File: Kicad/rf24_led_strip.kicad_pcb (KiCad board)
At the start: 2 copper layers, 50 x 50 mm, 85 parts, among them P1 12V in, P11 CONN_01X07, P2 LED_OUT, P3 LED2_OUT, P4 LED3_OUT, P5 LED4_OUT, P6 LED5_OUT, P7 USB_OTG, P8 SWD, P9 UART, Q10 Q_NMOS_GDS, Q11 Q_NMOS_GDS, Q12 Q_NMOS_GDS, Q13 Q_NMOS_GDS, Q14 Q_NMOS_GDS, Q15 Q_NMOS_GDS, Q16 Q_NMOS_GDS, Q2 Q_NMOS_GDS, Q3 Q_NMOS_GDS, Q4 Q_NMOS_GDS, Q5 Q_NMOS_GDS, Q6 Q_NMOS_GDS, Q7 Q_NMOS_GDS, Q8 Q_NMOS_GDS, Q9 Q_NMOS_GDS, U1 nrf24l01+, U2 ESP-01, U3 STM32F103C8Tx, U4 LM_1117, Y1 Crystal

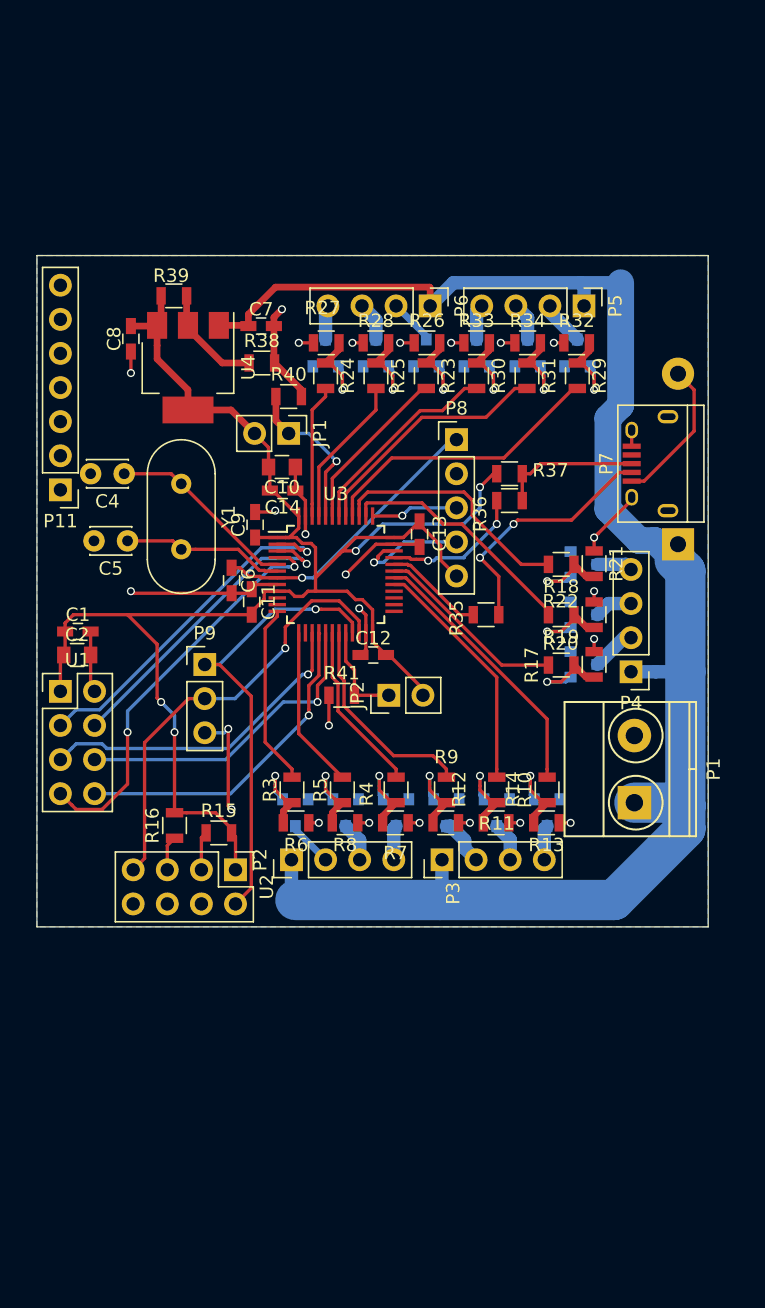
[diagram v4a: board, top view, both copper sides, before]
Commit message: First "complete" stm32 version.
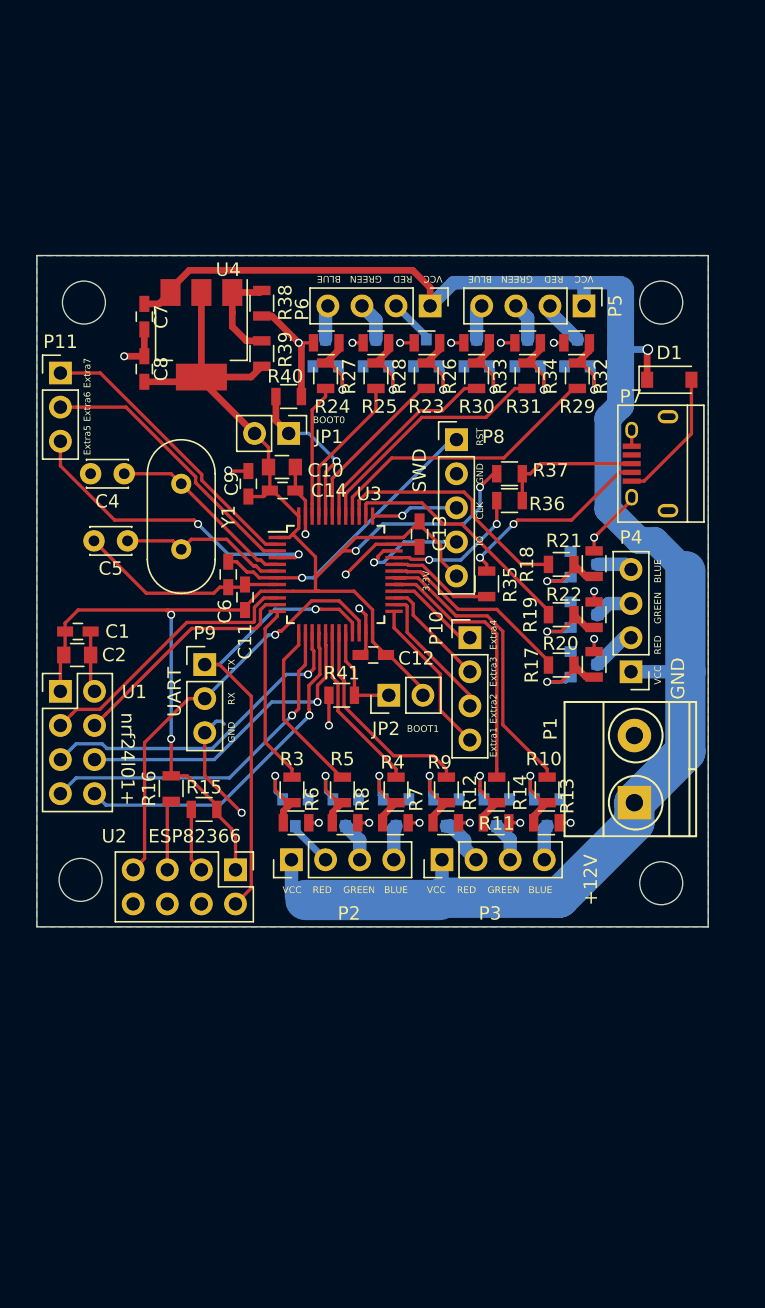
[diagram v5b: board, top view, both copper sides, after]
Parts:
- added P10: CONN_01X04, Pin_Headers:Pin_Header_Straight_1x04_Pitch2.54mm, F.Cu at (132.2, 78.5)
- added REF**: MountingHole_3.2mm_M3, Mounting_Holes:MountingHole_3.2mm_M3, F.Cu at (146.5, 53.5)
- added REF**: MountingHole_3.2mm_M3, Mounting_Holes:MountingHole_3.2mm_M3, F.Cu at (103.5, 53.5)
- added REF**: MountingHole_3.2mm_M3, Mounting_Holes:MountingHole_3.2mm_M3, F.Cu at (103.2, 96.5)
- added REF**: MountingHole_3.2mm_M3, Mounting_Holes:MountingHole_3.2mm_M3, F.Cu at (146.5, 96.8)
- added REF***: OSHW-Logo2_14.6x12mm_SilkScreen, Symbols:OSHW-Logo2_14.6x12mm_SilkScreen, B.Cu at (114.0, 56.5)
- C4, C5: value C -> 22pF
- C7, C8: value C -> 100nF
- D1: footprint Diodes_ThroughHole:D_DO-15_P12.70mm_Horizontal -> Diodes_SMD:D_SOD-123; moved to F.Cu
- P11: footprint Pin_Headers:Pin_Header_Straight_1x07_Pitch2.54mm -> Pin_Headers:Pin_Header_Straight_1x03_Pitch2.54mm
- R10, R11, R17, R18, R19, R23, R24, R25, R29, R3, R30, R31, R4, R5, R9: value R -> 1k
- R12, R13, R14, R15, R16, R20, R21, R22, R26, R27, R28, R32, R33, R34, R40, R41, R6, R7, R8: value R -> 10k
- R35, R36: value R -> 22Ω
- R37: value R -> 1.5k
- U4: value LM_1117 -> AMS1117
- moved D1 12.3 mm to (147.1, 59.2), turned to 0 degrees
- moved C7 8.73 mm to (108.0, 54.5), turned to 90 degrees
- moved P11 8.70 mm to (101.8, 58.8), turned to 0 degrees
- moved R39 7.84 mm to (116.8, 57.3), turned to 270 degrees
- moved R38 4.45 mm to (116.8, 53.5), turned to 270 degrees
- moved C9 3.09 mm to (115.8, 67.0)
- moved R16 2.76 mm to (110.0, 89.7)
- moved U4 2.65 mm to (112.2, 55.9)
- moved C8 2.46 mm to (108.0, 58.5), turned to 270 degrees
- moved R35 2.30 mm to (133.5, 74.5), turned to 270 degrees
- moved R15 2.07 mm to (112.5, 91.2)
- moved C11 0.61 mm to (115.5, 75.5)
- moved C6 0.51 mm to (114.2, 73.8)
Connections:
- P11 pad 1: /EXTRA1 -> /EXTRA7
- P11 pad 2: /EXTRA2 -> /EXTRA6
- P11 pad 3: /EXTRA3 -> /EXTRA5
- U3 pad 10: /EXTRA5 -> /CSN
- U3 pad 11: /EXTRA6 -> /CE
- U3 pad 14: /EXTRA7 -> /IRQ
- U3 pad 2: /CSN -> /EXTRA7
- U3 pad 3: /CE -> /EXTRA6
- U3 pad 4: /IRQ -> /EXTRA5
- U4 pad 1: +12V -> Net-(R38-Pad1)
- U4 pad 2: Net-(R38-Pad1) -> +3V3
- U4 pad 3: +3V3 -> +12V
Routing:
- net /EXTRA5: track 0.00 -> 24.0 mm, vias 0 -> 2
- net /EXTRA7: track 0.00 -> 21.7 mm
- net /EXTRA6: track 0.00 -> 20.8 mm
- net /EXTRA1: track 0.00 -> 11.9 mm
- net /EXTRA2: track 0.00 -> 10.4 mm
- net /EXTRA3: track 0.00 -> 8.42 mm
- net GND: track 71.3 -> 79.0 mm, vias 25 -> 22
- net /EXTRA4: track 0.00 -> 7.08 mm
- net /CE: track 23.7 -> 18.0 mm, vias 1 -> 0
- net /CSN: track 26.4 -> 20.7 mm, vias 1 -> 0
- net /IRQ: track 30.3 -> 26.2 mm, vias 2 -> 1
- net Net-(P7-Pad2): track 18.8 -> 15.1 mm
- net /BLUE2_PWM: track 20.1 -> 22.9 mm
- net Net-(R16-Pad1): track 2.57 -> 5.22 mm
- net /GREEN2_PWM: track 18.0 -> 20.6 mm
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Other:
- rule trace_min: 0.2 -> 0.25
- board text added: "+12V"
- board text added: "3.3V"
- board text added: "BLUE"
- board text added: "BOOT0"
- board text added: "BOOT1"
- board text added: "CLK"
- board text added: "ESP82366"
- board text added: "Extra1"
- board text added: "Extra2"
- board text added: "Extra3"
- board text added: "Extra4"
- board text added: "Extra5"
- board text added: "Extra6"
- board text added: "Extra7"
- board text added: "GND"
- board text added: "GREEN"
- board text added: "IO"
- board text added: "LED-Controller V0.1"
- board text added: "RED"
- board text added: "RST"
- board text added: "RX"
- board text added: "SWD"
- board text added: "TX"
- board text added: "UART"
- board text added: "VCC"
- board text added: "nrf24l01+"

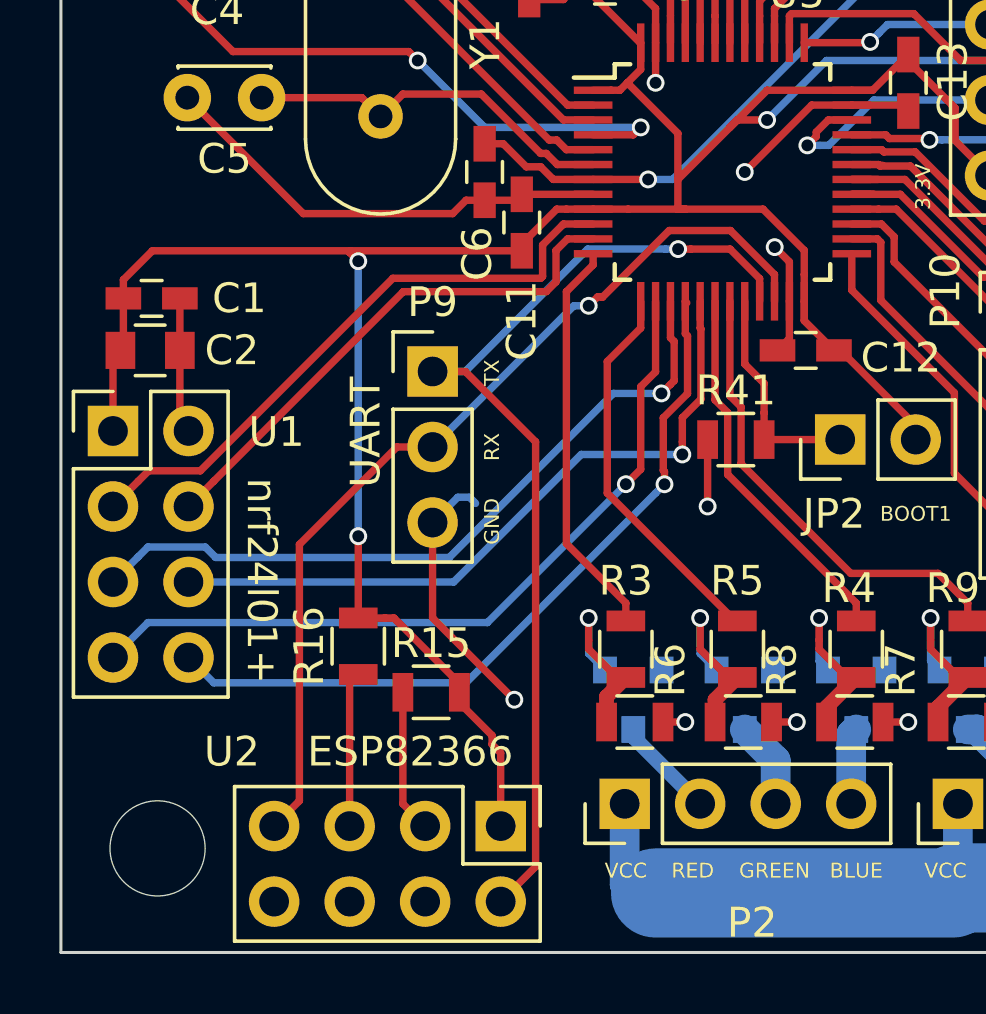
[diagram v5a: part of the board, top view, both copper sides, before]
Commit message: Fix wireless connectors.
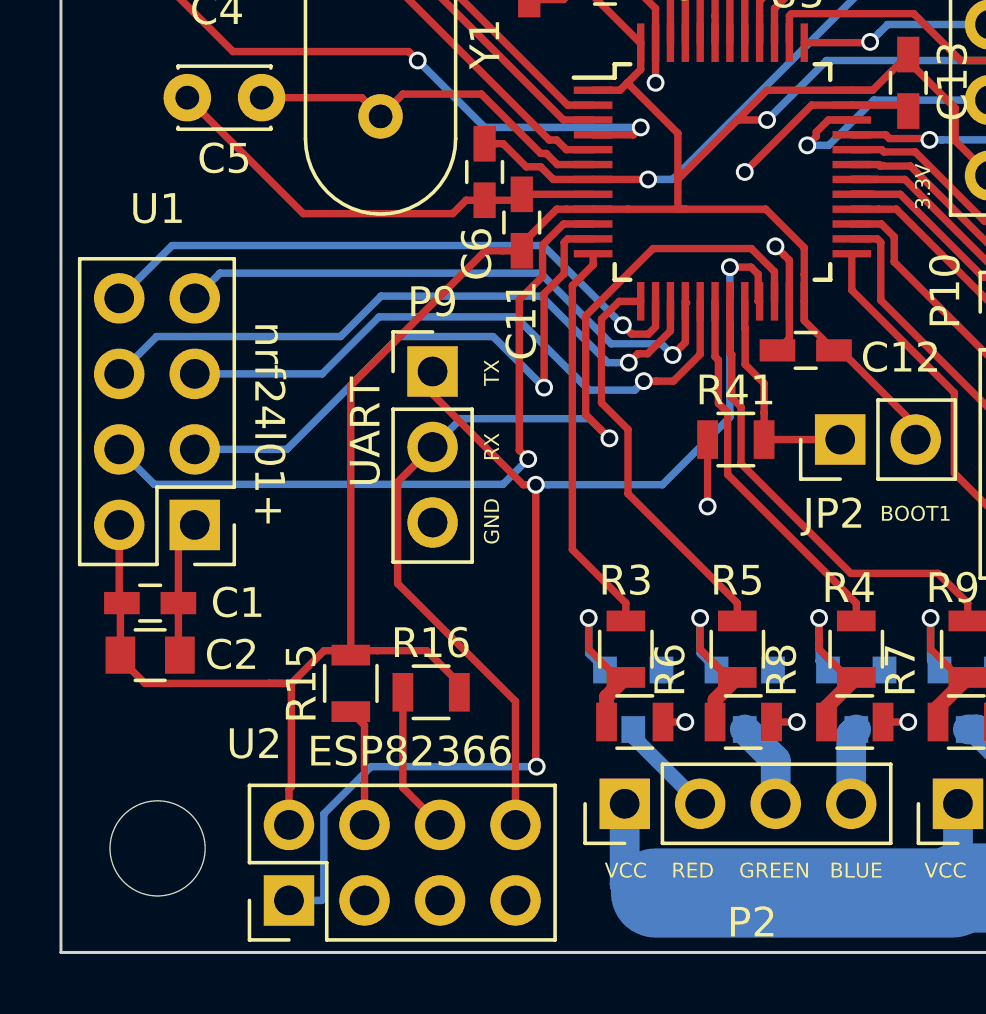
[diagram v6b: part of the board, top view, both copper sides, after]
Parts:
- moved C1 10.3 mm to (103.0, 88.2)
- moved C2 10.2 mm to (103.0, 90.0)
- moved U2 7.55 mm to (107.7, 98.2), turned to 90 degrees
- moved U1 4.19 mm to (104.5, 85.6), turned to 180 degrees
- moved R16 2.90 mm to (112.5, 91.2), turned to 0 degrees
- moved R15 2.72 mm to (109.8, 91.0), turned to 90 degrees
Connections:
- U1 pad 1: +3V3 -> GND
- U1 pad 2: GND -> +3V3
- U1 pad 3: /CSN -> /CE
- U1 pad 4: /CE -> /CSN
- U1 pad 5: /MOSI -> /SCK
- U1 pad 6: /SCK -> /MOSI
- U1 pad 7: /IRQ -> /MISO
- U1 pad 8: /MISO -> /IRQ
- U2 pad 1: +3V3 -> /TX
- U2 pad 2: /TX -> +3V3
- U2 pad 3: Net-(R15-Pad1) -> (no net)
- U2 pad 4: (no net) -> Net-(R15-Pad1)
- U2 pad 5: Net-(R16-Pad1) -> (no net)
- U2 pad 6: (no net) -> Net-(R16-Pad1)
- U2 pad 7: /RX -> GND
- U2 pad 8: GND -> /RX
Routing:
- net GND: track 79.0 -> 70.1 mm, vias 22 -> 21
- net /TX: track 34.3 -> 41.4 mm, vias 1 -> 3
- net /MISO: track 25.7 -> 19.6 mm
- net /IRQ: track 26.2 -> 21.0 mm
- net /CSN: track 20.7 -> 24.2 mm, vias 0 -> 1
- net /RX: track 31.7 -> 34.5 mm
- net /SCK: track 23.8 -> 21.1 mm
- net /MOSI: track 24.7 -> 22.0 mm
- net /CE: track 18.0 -> 20.2 mm, vias 0 -> 1
- net +3V3: track 128.5 -> 126.9 mm, vias 4 -> 2
- net Net-(R15-Pad1): track 4.81 -> 4.00 mm
- net /GREEN_PWM: track 13.1 -> 13.6 mm

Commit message: Fix micro usb.
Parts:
- P7: footprint Connect:USB_Micro-B -> Connectors_Molex:USB_Micro-B_Molex_47346-0001
- moved P7 1.60 mm to (147.2, 65.6), turned to 180 degrees
- moved R36 1.35 mm to (136.6, 68.2)
- moved R37 1.35 mm to (136.6, 66.2)
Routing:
- net GND: track 70.1 -> 82.8 mm
- net Net-(P7-Pad2): track 15.1 -> 16.7 mm
- net +3V3: track 126.9 -> 128.2 mm
- net /USB_DP: track 10.6 -> 11.1 mm
- net Net-(D1-Pad2): track 9.94 -> 10.2 mm, vias 0 -> 2
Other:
- board text added: "1"
- board text added: "2"
- board text added: "3"
- board text added: "4"
- board text added: "5"
- board text added: "6"
- board text added: "7"
- board text added: "B"
- board text added: "Extra"
- board text added: "G"
- board text added: "R"
- board text removed: "BLUE"
- board text removed: "Extra1"
- board text removed: "Extra2"
- board text removed: "Extra3"
- board text removed: "Extra4"
- board text removed: "Extra5"
- board text removed: "Extra6"
- board text removed: "Extra7"
- board text removed: "GREEN"
- board text removed: "RED"

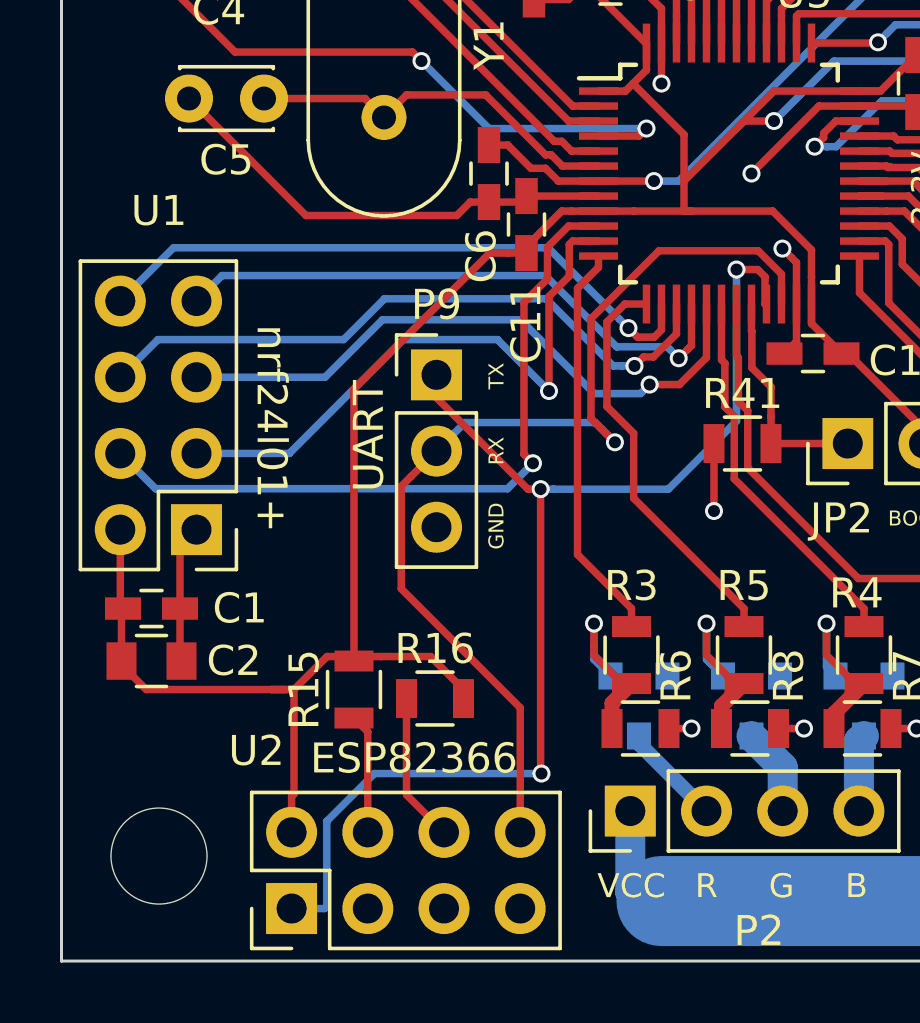
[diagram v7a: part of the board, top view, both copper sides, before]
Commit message: Fix spacing for ESP8266.
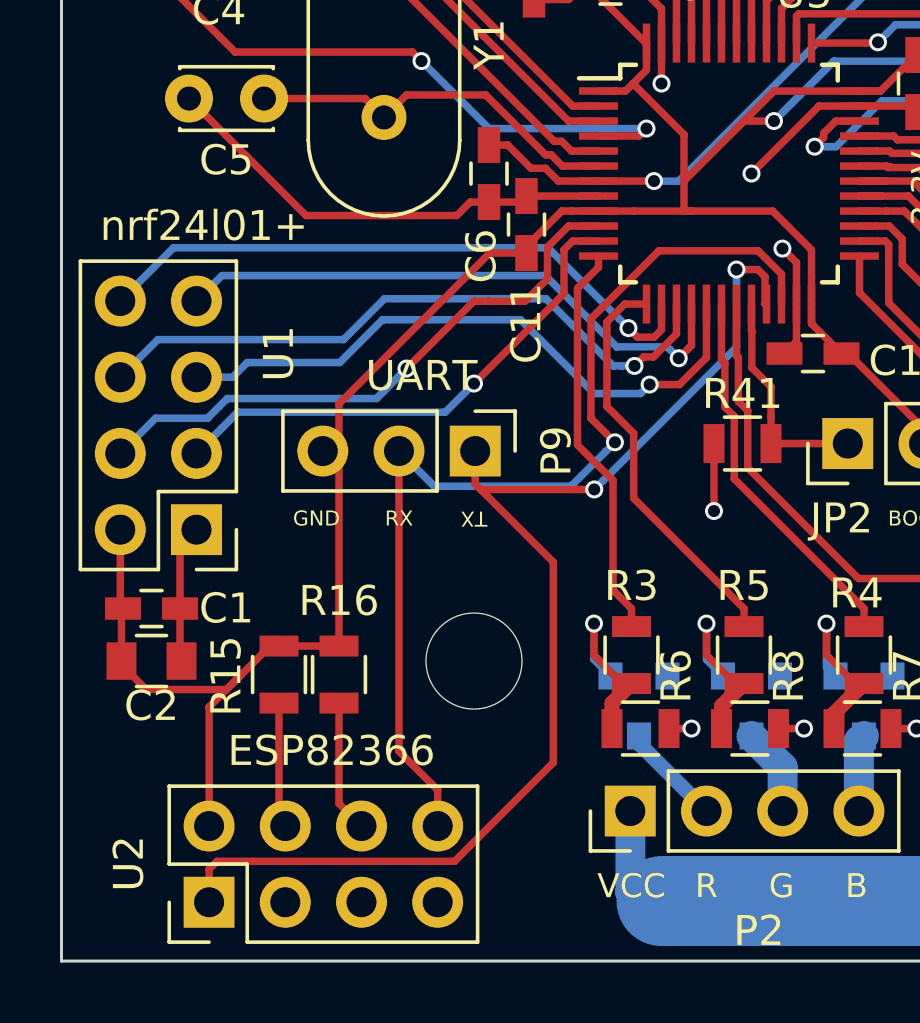
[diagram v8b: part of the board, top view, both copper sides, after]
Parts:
- moved REF** 12.3 mm to (113.8, 90.0)
- moved R16 3.30 mm to (109.2, 90.5), turned to 90 degrees
- moved P9 2.85 mm to (113.8, 83.0), turned to 270 degrees
- moved U2 2.76 mm to (104.9, 98.0)
- moved R15 2.55 mm to (107.2, 90.5)
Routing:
- net +3V3: track 128.2 -> 123.5 mm
- net /CSN: track 24.2 -> 19.7 mm
- net /CE: track 20.2 -> 17.2 mm
- net Net-(R16-Pad1): track 4.98 -> 4.41 mm
- net /TX: track 41.4 -> 40.9 mm, vias 3 -> 2
